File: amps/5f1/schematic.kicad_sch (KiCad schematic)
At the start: 26 parts, among them T2 SE 5k:8

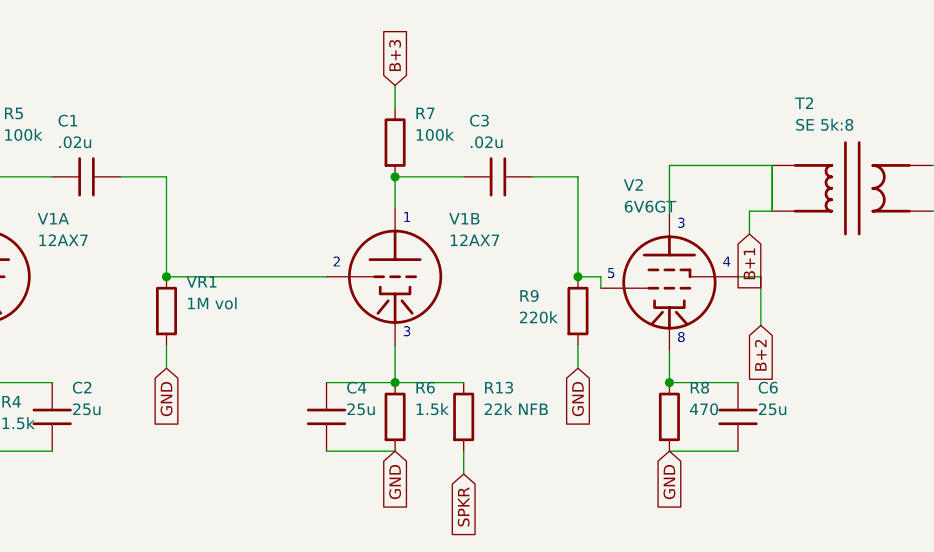
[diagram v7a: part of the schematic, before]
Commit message: Fix: 5F1 sheet drew its output transformer primary as a short and its volume control as a fixed resistor
Two faults on a verified sheet, found by a netlist-free cross-check of the
schematic against the board drawing (the two are authored independently, so
where they disagree at least one is wrong).

1. Five stray wire calls after the OT symbol — three of zero length and two
   spanning the primary pins — joined T2.1 to T2.2, so the plate, both
   primary pins, the first filter capacitor and the B+1 label were ONE net.
   The netlist gate could not object: sch_map anchors both primary pins to
   BP1, the DC model's own abstraction of the winding. Unique among the 44
   output transformers in the corpus. The wires are gone; T2.1 is now the
   plate's net and T2.2 the B+1 rail's.

2. VR1 was placed with the resistor symbol, so "1M vol" drew as a fixed 1 M
   from the grid node to ground with C1 tied straight to V1B's grid — a
   volume control that could not attenuate. It is now a potentiometer: C1 on
   the top lug, the wiper to the grid, the bottom lug grounded, which is what
   the board drawing already showed. One other sheet (5E6-A, VR3) draws a
   control with the resistor symbol; that one is a rheostat by design and
   goes to the sheet-vs-board triage rather than being changed blind.

Also the sheet's footnote no longer names repo files.

Gates: check_schematics 40/0 (connectivity 0 isolated pins); verify_schematic
_nets 5f1 PASS (claimed); validate 41/0; check_value_consistency --strict 0
disagreements; test_era_values 57; only the 5F1 sheet and its served copy
changed.

Co-Authored-By: Claude Fable 5.1 <noreply@anthropic.com>
Claude-Session: https://claude.ai/code/session_01KBMfdh37HmCL2iWcBiL5J1
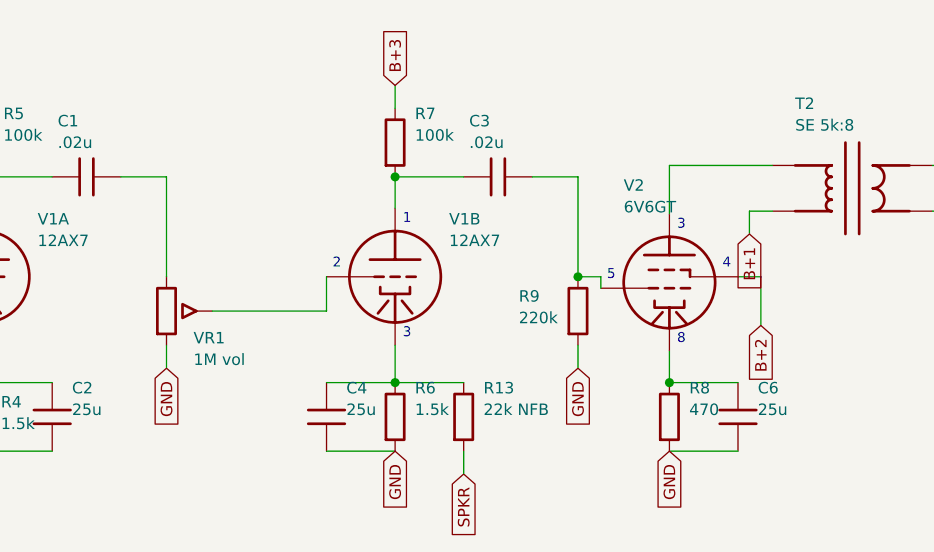
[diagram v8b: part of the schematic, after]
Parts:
- removed VR1: 1M vol, symbol cx:R
- added VR1: 1M vol, symbol cx:POT
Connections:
- net B+1: no longer T2.1 (PRI_P), V2.1 (P)
- net GND: now also VR1.3
- net at V1B.2 (G): now also VR1.2 (W); no longer C1.2
- new net: T2.1 (PRI_P), V2.1 (P)
- new net: C1.2, VR1.1
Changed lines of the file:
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@@
   (wire (pts (xy 67.0252 27.178) (xy 67.0252 38.278))
     (stroke (width 0) (type default)))
-  (junction (at 67.0252 38.278) (diameter 1) (color 0 0 0 0))
-  (symbol (lib_id "cx:R") (at 67.0252 42.088 0) (unit 1)
+  (symbol (lib_id "cx:POT") (at 67.0252 42.088 0) (unit 1)
     (in_bom yes) (on_board yes)
-    (property "Reference" "VR1" (at 69.2252 38.888 0) (effects (font (size 1.27 1.27)) (justify left)))
-    (property "Value" "1M vol" (at 69.2252 41.288 0) (effects (font (size 1.27 1.27)) (justify left))))
+    (property "Reference" "VR1" (at 70.0252 45.088 0) (effects (font (size 1.27 1.27)) (justify left)))
+    (property "Value" "1M vol" (at 70.0252 47.488 0) (effects (font (size 1.27 1.27)) (justify left))))
   (wire (pts (xy 67.0252 45.898) (xy 67.0252 48.438))
     (stroke (width 0) (type default)))
   (global_label "GND" (shape input) (at 67.0252 48.438 270)
     (effects (font (size 1.27 1.27)) (justify right)))
-  (wire (pts (xy 67.0252 38.278) (xy 84.8052 38.278))
+  (wire (pts (xy 72.1052 42.088) (xy 84.8052 42.088))
+    (stroke (width 0) (type default)))
+  (wire (pts (xy 84.8052 42.088) (xy 84.8052 38.278))
     (stroke (width 0) (type default)))
   (symbol (lib_id "cx:TRIODE") (at 92.4252 38.278 0) (unit 1)
@@
     (property "Reference" "T2" (at 136.875 19.048 0) (effects (font (size 1.27 1.27)) (justify left)))
     (property "Value" "SE 5k:8" (at 136.875 21.448 0) (effects (font (size 1.27 1.27)) (justify left))))
-  (wire (pts (xy 134.335 25.908) (xy 134.335 25.908))
-    (stroke (width 0) (type default)))
-  (wire (pts (xy 134.335 25.908) (xy 134.335 25.908))
-    (stroke (width 0) (type default)))
-  (wire (pts (xy 134.335 25.908) (xy 134.335 25.908))
-    (stroke (width 0) (type default)))
-  (wire (pts (xy 134.335 25.908) (xy 134.335 30.988))
-    (stroke (width 0) (type default)))
-  (wire (pts (xy 134.335 30.988) (xy 134.335 25.908))
-    (stroke (width 0) (type default)))
   (wire (pts (xy 134.335 30.988) (xy 131.795 30.988))
     (stroke (width 0) (type default)))
